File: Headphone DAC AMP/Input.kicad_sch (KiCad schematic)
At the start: 29 parts, among them J1 2137160001, J4 PINHD_1x2_Male, U2 XU316-1024-QF60B-C24, U8 W25Q16JVSNIQ

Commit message: "fuck my chud life"
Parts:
- F1: value 350mA -> 2A
- U2: footprint QFN_F60B-C24_XMO -> Package_DFN_QFN:QFN-60-1EP_7x7mm_P0.4mm_EP3.4x3.4mm_ThermalVias
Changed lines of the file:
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@@
 			)
 		)
-		(property "Value" "350mA"
+		(property "Value" "2A"
 			(at 40.64 22.86 90)
 			(effects
@@
 			)
 		)
-		(property "Footprint" "QFN_F60B-C24_XMO"
+		(property "Footprint" "Package_DFN_QFN:QFN-60-1EP_7x7mm_P0.4mm_EP3.4x3.4mm_ThermalVias"
 			(at 186.69 67.31 0)
 			(effects

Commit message: uPDATED fOOTPRINTS
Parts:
- U2: footprint Package_DFN_QFN:QFN-60-1EP_7x7mm_P0.4mm_EP3.4x3.4mm_ThermalVias -> footprints:QFN_F60B-C24_XMO
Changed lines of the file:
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@@
 			)
 		)
-		(property "Footprint" "Package_DFN_QFN:QFN-60-1EP_7x7mm_P0.4mm_EP3.4x3.4mm_ThermalVias"
+		(property "Footprint" "footprints:QFN_F60B-C24_XMO"
 			(at 186.69 67.31 0)
 			(effects

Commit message: uPDATED MORE FOOTPRINTS
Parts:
- added C100, C101, C102, C103: 100n, Capacitor_SMD:C_0402_1005Metric_Pad0.74x0.62mm_HandSolder, symbol Device:C
- C10, C11, C12, C13, C14, C15, C16, C17, C9, C96, C97, C98, C99: value 100nf -> 100n; footprint Capacitor_SMD:C_0805_2012Metric_Pad1.18x1.45mm_HandSolder -> Capacitor_SMD:C_0402_1005Metric_Pad0.74x0.62mm_HandSolder
- C18, C19: value 100nF -> 100n; footprint Capacitor_SMD:C_0805_2012Metric_Pad1.18x1.45mm_HandSolder -> Capacitor_SMD:C_0402_1005Metric_Pad0.74x0.62mm_HandSolder
- C56: footprint Capacitor_SMD:C_0805_2012Metric_Pad1.18x1.45mm_HandSolder -> Capacitor_SMD:C_0402_1005Metric_Pad0.74x0.62mm_HandSolder
- F1: footprint (none) -> Fuse:Fuse_0805_2012Metric_Pad1.15x1.40mm_HandSolder
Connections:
- net GND: now also C100.2, C101.2, C102.2, C103.2
- new net 1V8: C100.1, C101.1, C102.1, C103.1

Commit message: Cleaned up shcematic more
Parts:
- added FB2: 600R @ 100MHz, symbol Device:FerriteBead
- C103: value 100n -> 1u
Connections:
- net 0V9BP is gone; now on net 0V9: C10.1, C11.1, C12.1, C13.1, C14.1, C15.1, C16.1, C9.1, U2.12 (VDD), U2.19 (VDD), U2.27 (VDD), U2.34 (VDD), U2.4 (VDD), U2.42 (VDD), U2.49 (VDD), U2.57 (VDD), U2.61 (VDD), U2.62 (VDD), U2.63 (VDD), U2.64 (VDD)
- net 1V8_DBG is gone; now on net 1V8: U2.31 (USB_VDD18)
- net 1V8: now also U2.17 (VDDIOB18), U2.26 (VDDIOB18); no longer C103.1
- net PLL_AVDD: now reaches U2.22 (PLL_AVDD)
- net PLL_AVDD: now also C103.1, FB2.2
- new net PLL_0.9V: FB2.1
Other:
- note added: "5V Debug Input"
- note added: "Decoupling"
- note added: "QSPI Flash"
- note added: "Transient Protection"
- note added: "USB C Input"
- note added: "VBUS Filtering"
- note added: "XMOS XU316"
- moved on the sheet: C10, C100, C101, C102, C11, C12, C13, C14, C15, C16, C17, C9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

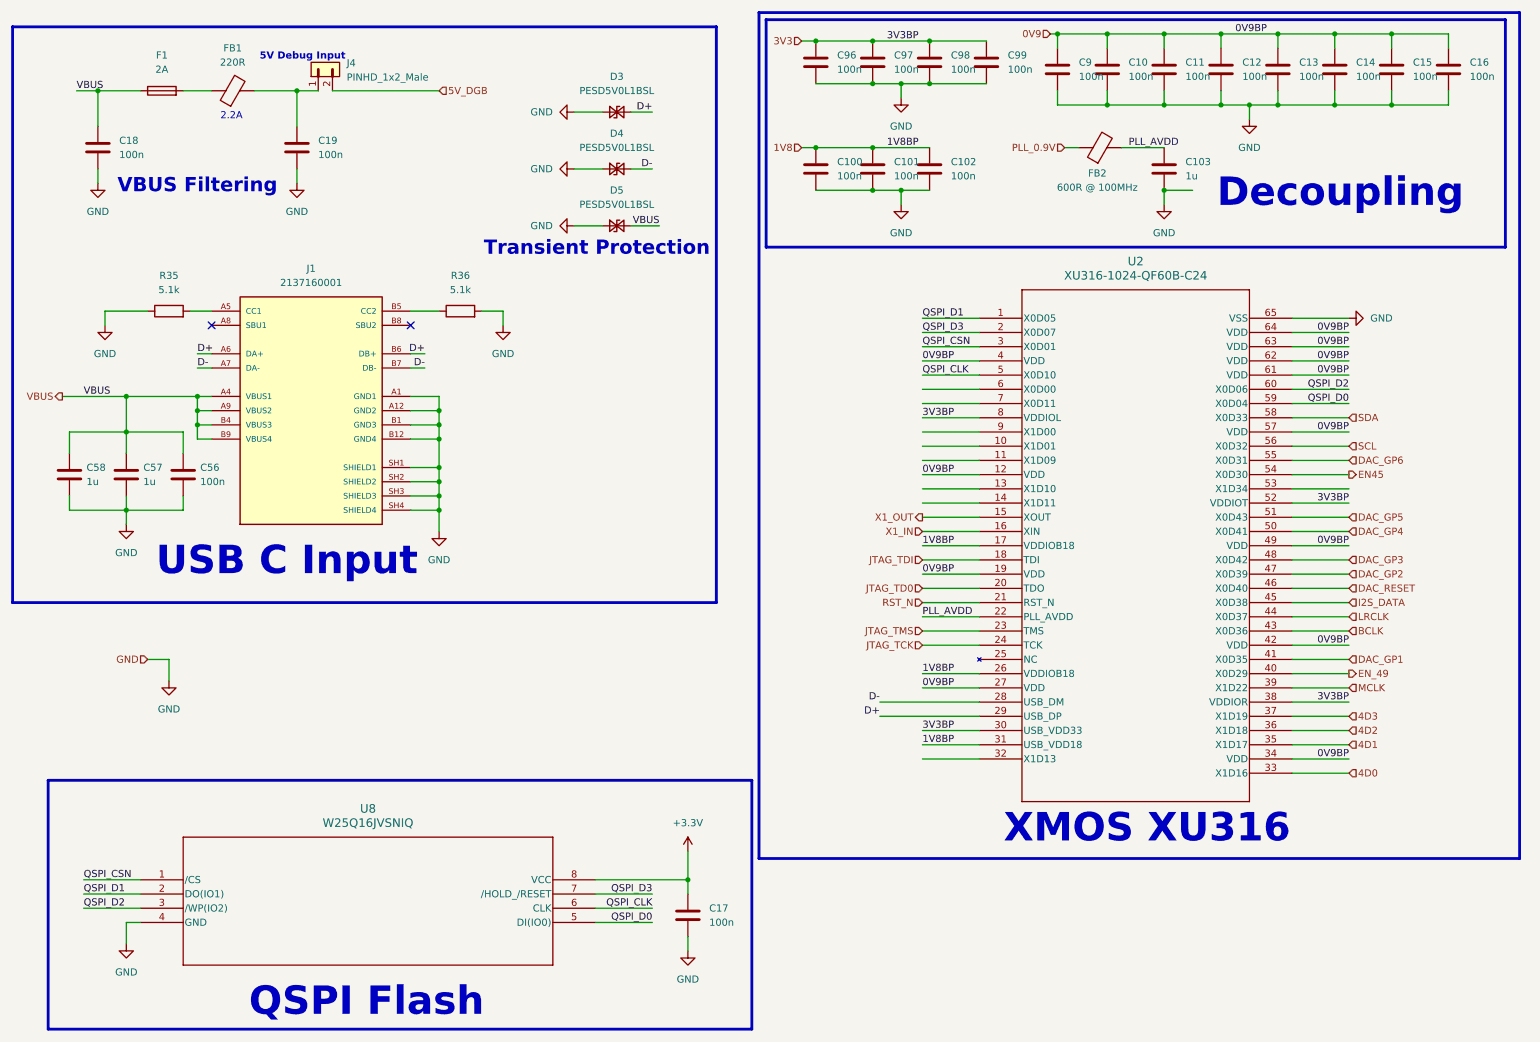
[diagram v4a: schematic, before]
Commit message: Cleaned Up and Annotated Schematic
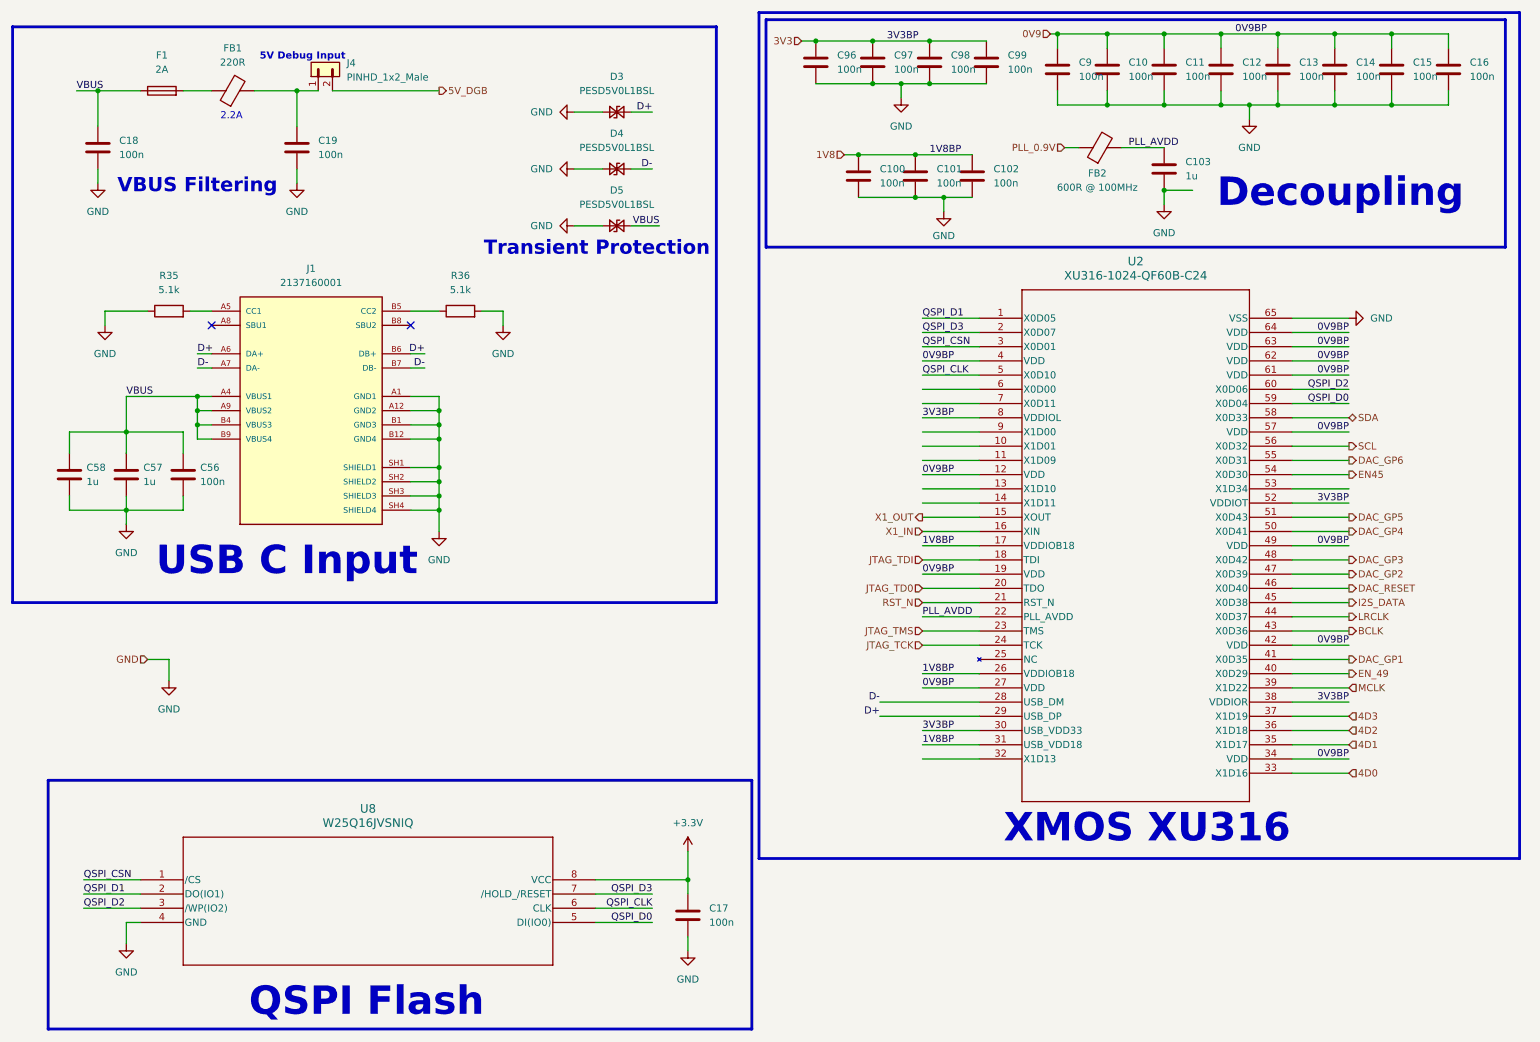
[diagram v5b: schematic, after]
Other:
- company: (none) -> Personal Project - Kettering University
- title: (none) -> Hi-Fidelity USB DAC Amplifier
- moved on the sheet: C100, C101, C102
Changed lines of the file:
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@@
 	(generator_version "9.0")
 	(paper "A4")
+	(title_block
+		(title "Hi-Fidelity USB DAC Amplifier")
+		(date "2025-11-19")
+		(rev "1.0")
+		(company "Personal Project - Kettering University")
+		(comment 1 "Designed by Dan Abidov & Luke Stirzinger")
+		(comment 2 "Based on XMOS Xu316 and ES9039Q2M")
+	)
 	(rectangle
 		(start 147.32 12.7)
@@
 	)
 	(junction
-		(at 172.72 44.45)
+		(at 180.34 45.72)
 		(diameter 0)
 		(color 0 0 0 0)
@@
 	)
 	(junction
-		(at 157.48 36.83)
+		(at 165.1 38.1)
 		(diameter 0)
 		(color 0 0 0 0)
@@
 	)
 	(junction
-		(at 167.64 44.45)
+		(at 175.26 45.72)
 		(diameter 0)
 		(color 0 0 0 0)
@@
 	)
 	(junction
-		(at 167.64 36.83)
+		(at 175.26 38.1)
 		(diameter 0)
 		(color 0 0 0 0)
@@
 	)
 	(junction
-		(at 34.29 81.28)
-		(diameter 0)
-		(color 0 0 0 0)
-	)
-	(junction
 		(at 46.99 83.82)
 		(diameter 0)
@@
 	(wire
 		(pts
-			(xy 157.48 36.83) (xy 167.64 36.83)
+			(xy 165.1 38.1) (xy 175.26 38.1)
 		)
 		(stroke
@@
 	(wire
 		(pts
-			(xy 157.48 44.45) (xy 167.64 44.45)
+			(xy 165.1 45.72) (xy 175.26 45.72)
 		)
 		(stroke
@@
 	(wire
 		(pts
-			(xy 172.72 44.45) (xy 172.72 46.99)
+			(xy 180.34 45.72) (xy 180.34 48.26)
 		)
 		(stroke
@@
 	(wire
 		(pts
-			(xy 167.64 36.83) (xy 177.8 36.83)
+			(xy 175.26 38.1) (xy 185.42 38.1)
 		)
 		(stroke
@@
 	(wire
 		(pts
-			(xy 167.64 44.45) (xy 172.72 44.45)
+			(xy 175.26 45.72) (xy 180.34 45.72)
 		)
 		(stroke
@@
 	(wire
 		(pts
-			(xy 22.86 81.28) (xy 34.29 81.28)
-		)
-		(stroke
-			(width 0)
-			(type default)
-		)
-	)
-	(wire
-		(pts
 			(xy 128.27 172.72) (xy 118.11 172.72)
 		)
@@
 	(wire
 		(pts
-			(xy 172.72 44.45) (xy 177.8 44.45)
+			(xy 180.34 45.72) (xy 185.42 45.72)
 		)
 		(stroke
@@
 	(wire
 		(pts
-			(xy 154.94 36.83) (xy 157.48 36.83)
+			(xy 162.56 38.1) (xy 165.1 38.1)
 		)
 		(stroke
@@
 	)
 	(label "1V8BP"
-		(at 170.18 36.83 0)
+		(at 177.8 38.1 0)
 		(effects
 			(font
@@
 	)
 	(label "VBUS"
-		(at 26.67 81.28 0)
+		(at 34.29 81.28 0)
 		(effects
 			(font
@@
 	)
 	(hierarchical_label "DAC_GP5"
-		(shape input)
+		(shape output)
 		(at 252.73 102.87 0)
 		(effects
@@
 	)
 	(hierarchical_label "DAC_GP1"
-		(shape input)
+		(shape output)
 		(at 252.73 128.27 0)
 		(effects
@@
 	)
 	(hierarchical_label "I2S_DATA"
-		(shape input)
+		(shape output)
 		(at 252.73 118.11 0)
 		(effects
@@
 	)
 	(hierarchical_label "SDA"
-		(shape input)
+		(shape bidirectional)
 		(at 252.73 85.09 0)
 		(effects
@@
 	)
 	(hierarchical_label "DAC_GP2"
-		(shape input)
+		(shape output)
 		(at 252.73 113.03 0)
 		(effects
@@
 	)
 	(hierarchical_label "5V_DGB"
-		(shape input)
+		(shape output)
 		(at 90.17 26.67 0)
 		(effects
@@
 	)
 	(hierarchical_label "LRCLK"
-		(shape input)
+		(shape output)
 		(at 252.73 120.65 0)
 		(effects
@@
 		)
 	)
-	(hierarchical_label "VBUS"
-		(shape output)
-		(at 22.86 81.28 180)
-		(effects
-			(font
-				(size 1.27 1.27)
-			)
-			(justify right)
-		)
-	)
 	(hierarchical_label "GND"
 		(shape input)
@@
 	)
 	(hierarchical_label "DAC_GP4"
-		(shape input)
+		(shape output)
 		(at 252.73 105.41 0)
 		(effects
@@
 	)
 	(hierarchical_label "DAC_GP3"
-		(shape input)
+		(shape output)
 		(at 252.73 110.49 0)
 		(effects
@@
 	)
 	(hierarchical_label "BCLK"
-		(shape input)
+		(shape output)
 		(at 252.73 123.19 0)
 		(effects
@@
 	)
 	(hierarchical_label "SCL"
-		(shape input)
+		(shape output)
 		(at 252.73 90.17 0)
 		(effects
@@
 	)
 	(hierarchical_label "DAC_GP6"
-		(shape input)
+		(shape output)
 		(at 252.73 92.71 0)
 		(effects
@@
 	(hierarchical_label "1V8"
 		(shape input)
-		(at 154.94 36.83 180)
+		(at 162.56 38.1 180)
 		(effects
 			(font
@@
 	)
 	(hierarchical_label "DAC_RESET"
-		(shape input)
+		(shape output)
 		(at 252.73 115.57 0)
 		(effects
@@
 	(symbol
 		(lib_id "Device:C")
-		(at 157.48 40.64 0)
+		(at 165.1 41.91 0)
 		(unit 1)
 		(exclude_from_sim no)
@@
 		(fields_autoplaced yes)
 		(property "Reference" "C100"
-			(at 161.29 39.3699 0)
+			(at 168.91 40.6399 0)
 			(effects
 				(font
@@
 		)
 		(property "Value" "100n"
-			(at 161.29 41.9099 0)
+			(at 168.91 43.1799 0)
 			(effects
 				(font
@@
 		)
 		(property "Footprint" "Capacitor_SMD:C_0402_1005Metric_Pad0.74x0.62mm_HandSolder"
-			(at 158.4452 44.45 0)
+			(at 166.0652 45.72 0)
 			(effects
 				(font
@@
 		)
 		(property "Datasheet" "~"
-			(at 157.48 40.64 0)
+			(at 165.1 41.91 0)
 			(effects
 				(font
@@
 		)
 		(property "Description" "Unpolarized capacitor"
-			(at 157.48 40.64 0)
+			(at 165.1 41.91 0)
 			(effects
 				(font
@@
 	(symbol
 		(lib_id "Device:C")
-		(at 177.8 40.64 0)
+		(at 185.42 41.91 0)
 		(unit 1)
 		(exclude_from_sim no)
@@
 		(fields_autoplaced yes)
 		(property "Reference" "C102"
-			(at 181.61 39.3699 0)
+			(at 189.23 40.6399 0)
 			(effects
 				(font
@@
 		)
 		(property "Value" "100n"
-			(at 181.61 41.9099 0)
+			(at 189.23 43.1799 0)
 			(effects
 				(font
@@
 		)
 		(property "Footprint" "Capacitor_SMD:C_0402_1005Metric_Pad0.74x0.62mm_HandSolder"
-			(at 178.7652 44.45 0)
+			(at 186.3852 45.72 0)
 			(effects
 				(font
@@
 		)
 		(property "Datasheet" "~"
-			(at 177.8 40.64 0)
+			(at 185.42 41.91 0)
 			(effects
 				(font
@@
 		)
 		(property "Description" "Unpolarized capacitor"
-			(at 177.8 40.64 0)
+			(at 185.42 41.91 0)
 			(effects
 				(font
@@
 	(symbol
 		(lib_id "Device:C")
-		(at 167.64 40.64 0)
+		(at 175.26 41.91 0)
 		(unit 1)
 		(exclude_from_sim no)
@@
 		(fields_autoplaced yes)
 		(property "Reference" "C101"
-			(at 171.45 39.3699 0)
+			(at 179.07 40.6399 0)
 			(effects
 				(font
@@
 		)
 		(property "Value" "100n"
-			(at 171.45 41.9099 0)
+			(at 179.07 43.1799 0)
 			(effects
 				(font
@@
 		)
 		(property "Footprint" "Capacitor_SMD:C_0402_1005Metric_Pad0.74x0.62mm_HandSolder"
-			(at 168.6052 44.45 0)
+			(at 176.2252 45.72 0)
 			(effects
 				(font
@@
 		)
 		(property "Datasheet" "~"
-			(at 167.64 40.64 0)
+			(at 175.26 41.91 0)
 			(effects
 				(font
@@
 		)
 		(property "Description" "Unpolarized capacitor"
-			(at 167.64 40.64 0)
+			(at 175.26 41.91 0)
 			(effects
 				(font
@@
 	(symbol
 		(lib_id "power:GND")
-		(at 172.72 46.99 0)
+		(at 180.34 48.26 0)
 		(unit 1)
 		(exclude_from_sim no)
@@
 		(on_board yes)
 		(dnp no)
-		(fields_autoplaced yes)
 		(property "Reference" "#PWR0110"
-			(at 172.72 53.34 0)
+			(at 180.34 54.61 0)
 			(effects
 				(font
@@
 		)
 		(property "Value" "GND"
-			(at 172.72 52.07 0)
+			(at 180.34 52.578 0)
 			(effects
 				(font
@@
 		)
 		(property "Footprint" ""
-			(at 172.72 46.99 0)
+			(at 180.34 48.26 0)
 			(effects
 				(font
@@
 		)
 		(property "Datasheet" ""
-			(at 172.72 46.99 0)
+			(at 180.34 48.26 0)
 			(effects
 				(font
@@
 		)
 		(property "Description" "Power symbol creates a global label with name \"GND\" , ground"
-			(at 172.72 46.99 0)
+			(at 180.34 48.26 0)
 			(effects
 				(font

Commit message: Schematic V1 Done
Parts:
- FB1: footprint (none) -> Capacitor_SMD:C_0805_2012Metric_Pad1.18x1.45mm_HandSolder
- FB2: footprint (none) -> Capacitor_SMD:C_0603_1608Metric_Pad1.08x0.95mm_HandSolder
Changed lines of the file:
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@@
 			)
 		)
-		(property "Footprint" ""
+		(property "Footprint" "Capacitor_SMD:C_0805_2012Metric_Pad1.18x1.45mm_HandSolder"
 			(at 53.34 28.448 90)
 			(effects
@@
 			)
 		)
-		(property "Footprint" ""
+		(property "Footprint" "Capacitor_SMD:C_0603_1608Metric_Pad1.08x0.95mm_HandSolder"
 			(at 208.28 38.608 90)
 			(effects

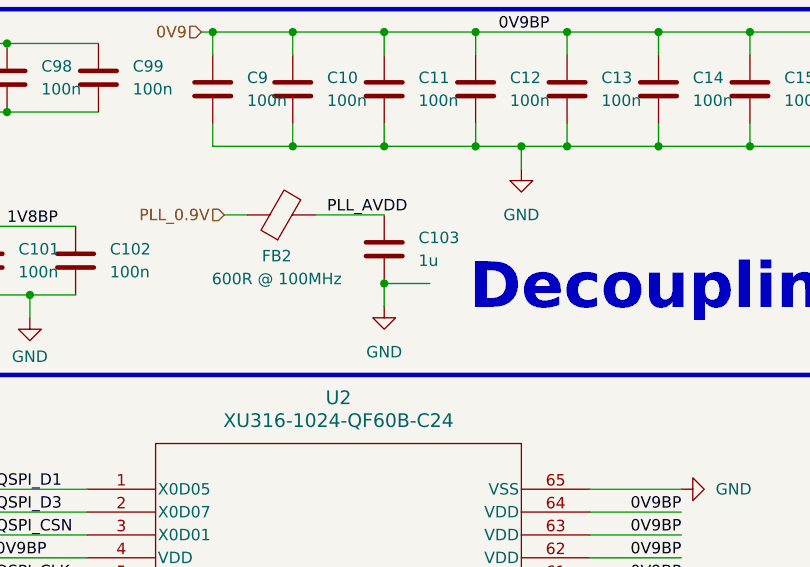
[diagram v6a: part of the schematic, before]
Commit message: Footprints & Placements
All footprints are loaded in PCB error free, some PCB mistakes were fixed, and worked on the placements for the TPA6120, the XMOS, the DAC, and the outputs
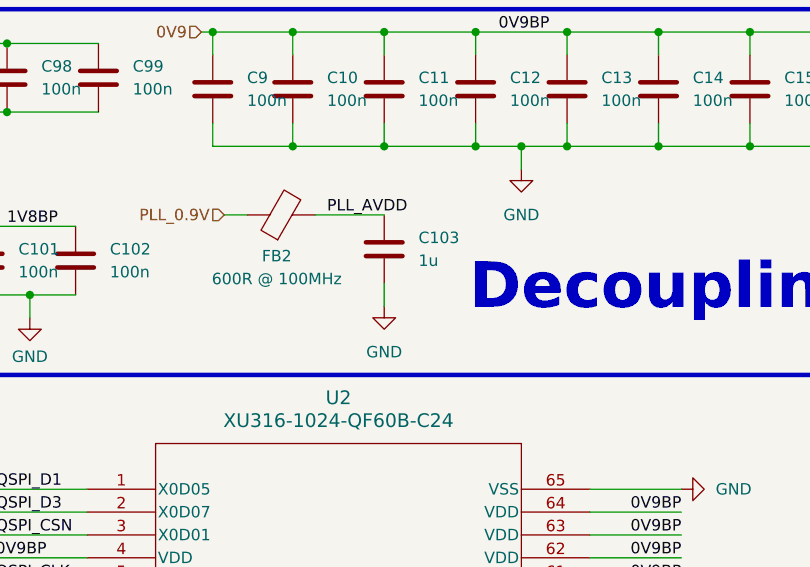
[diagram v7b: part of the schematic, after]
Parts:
- U8: footprint SOIC_150MIL_WIN -> W25Q16JVSNIQ:SOIC_150MIL_WIN
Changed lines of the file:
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@@
 	)
 	(junction
-		(at 219.71 44.45)
-		(diameter 0)
-		(color 0 0 0 0)
-	)
-	(junction
 		(at 134.62 167.64)
 		(diameter 0)
@@
 	(wire
 		(pts
-			(xy 219.71 44.45) (xy 224.79 44.45)
-		)
-		(stroke
-			(width 0)
-			(type default)
-		)
-	)
-	(wire
-		(pts
 			(xy 270.51 16.51) (xy 260.35 16.51)
 		)
@@
 			)
 		)
-		(property "Footprint" "SOIC_150MIL_WIN"
+		(property "Footprint" "W25Q16JVSNIQ:SOIC_150MIL_WIN"
 			(at 36.83 167.64 0)
 			(effects

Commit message: Swapped to 0603 caps in order to compact design
Planning on a 100x70mm board shape
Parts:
- C57, C58: footprint Capacitor_SMD:C_0805_2012Metric_Pad1.18x1.45mm_HandSolder -> Capacitor_SMD:C_0603_1608Metric_Pad1.08x0.95mm_HandSolder
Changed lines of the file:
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@@
 			)
 		)
-		(property "Footprint" "Capacitor_SMD:C_0805_2012Metric_Pad1.18x1.45mm_HandSolder"
+		(property "Footprint" "Capacitor_SMD:C_0603_1608Metric_Pad1.08x0.95mm_HandSolder"
 			(at 35.2552 99.06 0)
 			(effects
@@
 			)
 		)
-		(property "Footprint" "Capacitor_SMD:C_0805_2012Metric_Pad1.18x1.45mm_HandSolder"
+		(property "Footprint" "Capacitor_SMD:C_0603_1608Metric_Pad1.08x0.95mm_HandSolder"
 			(at 25.0952 99.06 0)
 			(effects
